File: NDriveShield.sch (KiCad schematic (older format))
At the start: 26 parts, among them Q1 NTD5867NLT4G, Q2 NTD5867NLT4G, Q3 NTD5867NLT4G, Q4 NTD5867NLT4G, Q5 NTD5867NLT4G, Q6 NTD5867NLT4G, SW1 SW_PUSHBUTTON

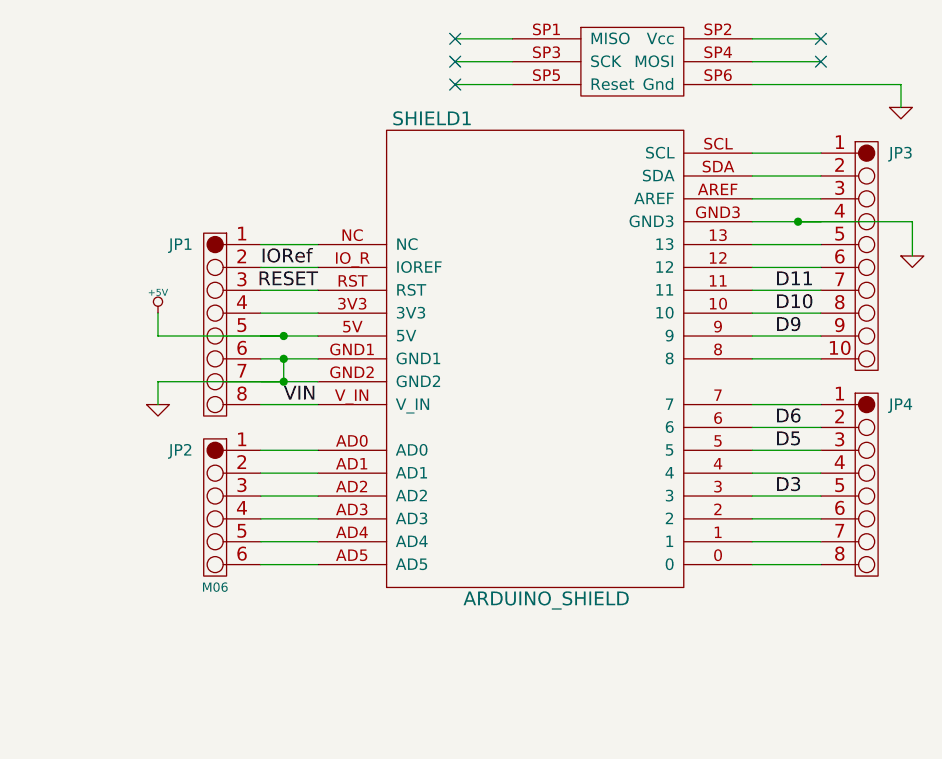
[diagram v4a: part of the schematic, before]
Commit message: Bump to V1.1, change appearance to FT-style breakout pads.
Closes #2
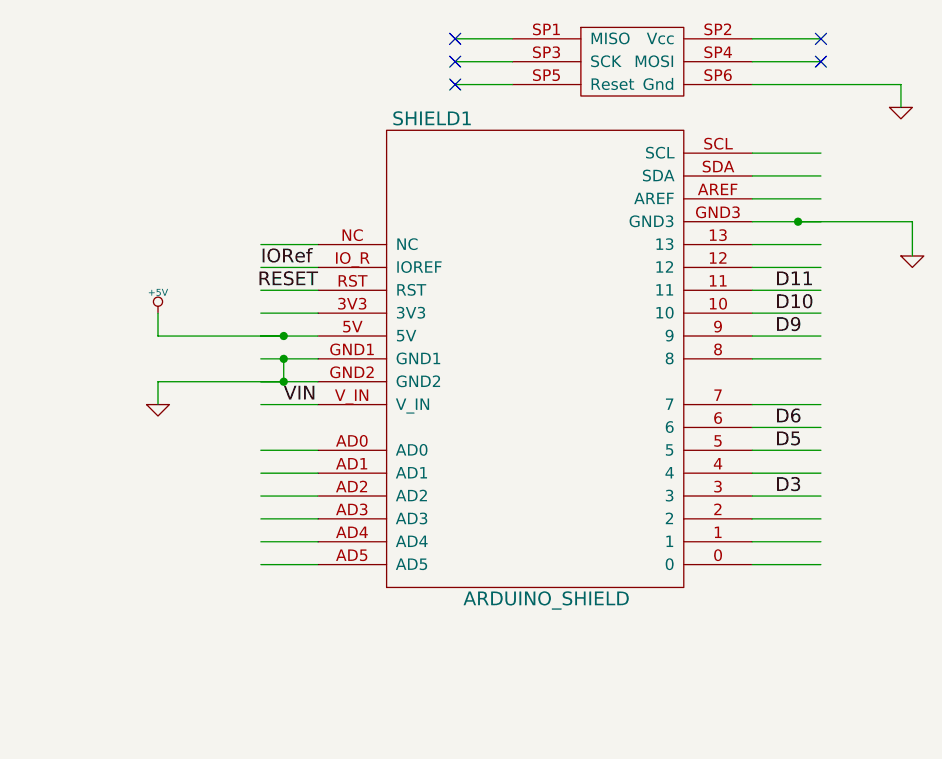
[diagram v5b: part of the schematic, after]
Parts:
- removed JP1, JP4: M08, symbol M08
- removed JP2: M06, symbol M06
- removed JP3: M10, symbol M10
- JP5: footprint (none) -> FT:TERMINALBLOCK_3.5MM_8
- LED1, LED2, LED3, LED4, LED5, LED6, LED7: footprint (none) -> FT:LED-0603
- Q1, Q2, Q3, Q4, Q5, Q6: footprint (none) -> FT:MOSFET_DPAK
- R1, R2, R3, R4, R5, R6: footprint (none) -> FT:RES_CAY16
- SHIELD1: footprint (none) -> FT:ARDUINO_SHIELD_ROUNDPADS_BREAKOUT
- SW1: footprint (none) -> FT:TACTILE_SWITCH_SMD_2PIN_TINY
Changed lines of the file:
@@
 EESchema Schematic File Version 2
-LIBS:freetronics_kicad_sch_lib
+LIBS:freetronics_schematic
 LIBS:power
 LIBS:device
@@
 F 0 "SHIELD1" H 8800 3800 60  0000 C CNN
 F 1 "ARDUINO_SHIELD" H 9300 1700 60  0000 C CNN
-F 2 "" H 9250 2650 60  0000 C CNN
+F 2 "FT:ARDUINO_SHIELD_ROUNDPADS_BREAKOUT" H 9250 2650 60  0001 C CNN
 F 3 "" H 9250 2650 60  0000 C CNN
 	1    9250 2650
 	1    0    0    -1
-$EndComp
-$Comp
-L M08 JP4
-U 1 1 53BDDB94
-P 10800 2750
-F 0 "JP4" H 10850 2750 50  0000 C CNN
-F 1 "M08" H 10700 1950 40  0001 C CNN
-F 2 "" H 10800 2750 60  0000 C CNN
-F 3 "" H 10800 2750 60  0000 C CNN
-	1    10800 2750
-	1    0    0    -1
-$EndComp
-$Comp
-L M10 JP3
-U 1 1 53BDDBD8
-P 10800 1650
-F 0 "JP3" H 10850 1650 50  0000 C CNN
-F 1 "M10" H 10700 650 40  0001 C CNN
-F 2 "" H 10800 1650 60  0000 C CNN
-F 3 "" H 10800 1650 60  0000 C CNN
-	1    10800 1650
-	1    0    0    -1
-$EndComp
-$Comp
-L M06 JP2
-U 1 1 53BDDD8A
-P 7750 2950
-F 0 "JP2" H 7800 2950 50  0000 C CNN
-F 1 "M06" H 7650 2350 40  0000 C CNN
-F 2 "" H 7750 2950 60  0000 C CNN
-F 3 "" H 7750 2950 60  0000 C CNN
-	1    7750 2950
-	-1   0    0    -1
-$EndComp
-$Comp
-L M08 JP1
-U 1 1 53BDDE77
-P 7750 2050
-F 0 "JP1" H 7800 2050 50  0000 C CNN
-F 1 "M08" H 7650 1250 40  0001 C CNN
-F 2 "" H 7750 2050 60  0000 C CNN
-F 3 "" H 7750 2050 60  0000 C CNN
-	1    7750 2050
-	-1   0    0    -1
 $EndComp
 Text Label 10300 3150 0    60   ~ 0
@@
 F 0 "JP5" H 1050 1650 50  0000 C CNN
 F 1 "M08" H 1050 750 40  0000 C CNN
-F 2 "" H 1150 1550 60  0000 C CNN
+F 2 "FT:TERMINALBLOCK_3.5MM_8" H 1150 1550 60  0001 C CNN
 F 3 "" H 1150 1550 60  0000 C CNN
 	1    1150 1550
@@
 F 0 "LED1" H 3850 2700 50  0000 C CNN
 F 1 "LED" H 3850 2500 50  0000 C CNN
-F 2 "" H 3850 2600 60  0000 C CNN
+F 2 "FT:LED-0603" H 3850 2400 60  0001 C CNN
 F 3 "" H 3850 2600 60  0000 C CNN
 	1    3850 2600
@@
 F 0 "R1" H 3350 1700 50  0000 C CNN
 F 1 "1K" H 3350 1800 50  0000 C CNN
-F 2 "" H 3350 1800 60  0000 C CNN
+F 2 "FT:RES_CAY16" H 3350 1800 60  0001 C CNN
 F 3 "" H 3350 1800 60  0000 C CNN
 	1    3350 1800
@@
 F 0 "R3" H 3850 2250 50  0000 C CNN
 F 1 "10K" H 3850 2150 50  0000 C CNN
-F 2 "" H 3850 2150 60  0000 C CNN
+F 2 "FT:RES_CAY16" H 3850 2150 60  0001 C CNN
 F 3 "" H 3850 2150 60  0000 C CNN
 	1    3850 2150
@@
 F 0 "R2" H 3050 2250 50  0000 C CNN
 F 1 "470R" H 3050 2150 50  0000 C CNN
-F 2 "" H 3050 2150 60  0000 C CNN
+F 2 "FT:RES_CAY16" H 3050 2150 60  0001 C CNN
 F 3 "" H 3050 2150 60  0000 C CNN
 	3    3050 2150
@@
 F 0 "Q1" H 4000 1700 60  0000 R CNN
 F 1 "NTD5867NLT4G" V 4400 2050 60  0000 R CNN
-F 2 "" H 4100 1800 60  0000 C CNN
+F 2 "FT:MOSFET_DPAK" H 4100 1800 60  0001 C CNN
 F 3 "" H 4100 1800 60  0000 C CNN
 	1    4100 1800
@@
 F 0 "LED2" H 3850 4350 50  0000 C CNN
 F 1 "LED" H 3850 4150 50  0000 C CNN
-F 2 "" H 3850 4250 60  0000 C CNN
+F 2 "FT:LED-0603" H 3850 4250 60  0001 C CNN
 F 3 "" H 3850 4250 60  0000 C CNN
 	1    3850 4250
@@
 F 0 "R1" H 3350 3350 50  0000 C CNN
 F 1 "1K" H 3350 3450 50  0000 C CNN
-F 2 "" H 3350 3450 60  0000 C CNN
+F 2 "FT:RES_CAY16" H 3350 3450 60  0001 C CNN
 F 3 "" H 3350 3450 60  0000 C CNN
 	2    3350 3450
@@
 F 0 "R3" H 3850 3900 50  0000 C CNN
 F 1 "10K" H 3850 3800 50  0000 C CNN
-F 2 "" H 3850 3800 60  0000 C CNN
+F 2 "FT:RES_CAY16" H 3850 3800 60  0001 C CNN
 F 3 "" H 3850 3800 60  0000 C CNN
 	2    3850 3800
@@
 F 0 "R2" H 3050 3900 50  0000 C CNN
 F 1 "470R" H 3050 3800 50  0000 C CNN
-F 2 "" H 3050 3800 60  0000 C CNN
+F 2 "FT:RES_CAY16" H 3050 3800 60  0001 C CNN
 F 3 "" H 3050 3800 60  0000 C CNN
 	2    3050 3800
@@
 F 0 "Q2" H 4000 3350 60  0000 R CNN
 F 1 "NTD5867NLT4G" V 4400 3700 60  0000 R CNN
-F 2 "" H 4100 3450 60  0000 C CNN
+F 2 "FT:MOSFET_DPAK" H 4100 3450 60  0001 C CNN
 F 3 "" H 4100 3450 60  0000 C CNN
 	1    4100 3450
@@
 F 0 "LED4" H 6050 2700 50  0000 C CNN
 F 1 "LED" H 6050 2500 50  0000 C CNN
-F 2 "" H 6050 2600 60  0000 C CNN
+F 2 "FT:LED-0603" H 6050 2400 60  0001 C CNN
 F 3 "" H 6050 2600 60  0000 C CNN
 	1    6050 2600
@@
 F 0 "R1" H 5550 1700 50  0000 C CNN
 F 1 "1K" H 5550 1800 50  0000 C CNN
-F 2 "" H 5550 1800 60  0000 C CNN
+F 2 "FT:RES_CAY16" H 5550 1800 60  0001 C CNN
 F 3 "" H 5550 1800 60  0000 C CNN
 	4    5550 1800
@@
 F 0 "R3" H 6050 2250 50  0000 C CNN
 F 1 "10K" H 6050 2150 50  0000 C CNN
-F 2 "" H 6050 2150 60  0000 C CNN
+F 2 "FT:RES_CAY16" H 6050 2150 60  0001 C CNN
 F 3 "" H 6050 2150 60  0000 C CNN
 	4    6050 2150
@@
 F 0 "R5" H 5250 2250 50  0000 C CNN
 F 1 "470R" H 5250 2150 50  0000 C CNN
-F 2 "" H 5250 2150 60  0000 C CNN
+F 2 "FT:RES_CAY16" H 5250 2150 60  0001 C CNN
 F 3 "" H 5250 2150 60  0000 C CNN
 	3    5250 2150
@@
 F 0 "Q4" H 6200 1700 60  0000 R CNN
 F 1 "NTD5867NLT4G" V 6600 2050 60  0000 R CNN
-F 2 "" H 6300 1800 60  0000 C CNN
+F 2 "FT:MOSFET_DPAK" H 6300 1800 60  0001 C CNN
 F 3 "" H 6300 1800 60  0000 C CNN
 	1    6300 1800
@@
 F 0 "LED5" H 6050 4350 50  0000 C CNN
 F 1 "LED" H 6050 4150 50  0000 C CNN
-F 2 "" H 6050 4250 60  0000 C CNN
+F 2 "FT:LED-0603" H 6050 4250 60  0001 C CNN
 F 3 "" H 6050 4250 60  0000 C CNN
 	1    6050 4250
@@
 F 0 "R4" H 5550 3350 50  0000 C CNN
 F 1 "1K" H 5550 3450 50  0000 C CNN
-F 2 "" H 5550 3450 60  0000 C CNN
+F 2 "FT:RES_CAY16" H 5550 3450 60  0001 C CNN
 F 3 "" H 5550 3450 60  0000 C CNN
 	2    5550 3450
@@
 F 0 "R6" H 6050 3900 50  0000 C CNN
 F 1 "10K" H 6050 3800 50  0000 C CNN
-F 2 "" H 6050 3800 60  0000 C CNN
+F 2 "FT:RES_CAY16" H 6050 3800 60  0001 C CNN
 F 3 "" H 6050 3800 60  0000 C CNN
 	2    6050 3800
@@
 F 0 "R5" H 5250 3900 50  0000 C CNN
 F 1 "470R" H 5250 3800 50  0000 C CNN
-F 2 "" H 5250 3800 60  0000 C CNN
+F 2 "FT:RES_CAY16" H 5250 3800 60  0001 C CNN
 F 3 "" H 5250 3800 60  0000 C CNN
 	2    5250 3800
@@
 F 0 "Q5" H 6200 3350 60  0000 R CNN
 F 1 "NTD5867NLT4G" V 6600 3700 60  0000 R CNN
-F 2 "" H 6300 3450 60  0000 C CNN
+F 2 "FT:MOSFET_DPAK" H 6300 3450 60  0001 C CNN
 F 3 "" H 6300 3450 60  0000 C CNN
 	1    6300 3450
@@
 F 0 "LED3" H 3850 6000 50  0000 C CNN
 F 1 "LED" H 3850 5800 50  0000 C CNN
-F 2 "" H 3850 5900 60  0000 C CNN
+F 2 "FT:LED-0603" H 3850 5900 60  0001 C CNN
 F 3 "" H 3850 5900 60  0000 C CNN
 	1    3850 5900
@@
 F 0 "R1" H 3350 5000 50  0000 C CNN
 F 1 "1K" H 3350 5100 50  0000 C CNN
-F 2 "" H 3350 5100 60  0000 C CNN
+F 2 "FT:RES_CAY16" H 3350 5100 60  0001 C CNN
 F 3 "" H 3350 5100 60  0000 C CNN
 	3    3350 5100
@@
 F 0 "R3" H 3850 5550 50  0000 C CNN
 F 1 "10K" H 3850 5450 50  0000 C CNN
-F 2 "" H 3850 5450 60  0000 C CNN
+F 2 "FT:RES_CAY16" H 3850 5450 60  0001 C CNN
 F 3 "" H 3850 5450 60  0000 C CNN
 	3    3850 5450
@@
 F 0 "R2" H 3050 5550 50  0000 C CNN
 F 1 "470R" H 3050 5450 50  0000 C CNN
-F 2 "" H 3050 5450 60  0000 C CNN
+F 2 "FT:RES_CAY16" H 3050 5450 60  0001 C CNN
 F 3 "" H 3050 5450 60  0000 C CNN
 	1    3050 5450
@@
 F 0 "Q3" H 4000 5000 60  0000 R CNN
 F 1 "NTD5867NLT4G" V 4400 5350 60  0000 R CNN
-F 2 "" H 4100 5100 60  0000 C CNN
+F 2 "FT:MOSFET_DPAK" H 4100 5100 60  0001 C CNN
 F 3 "" H 4100 5100 60  0000 C CNN
 	1    4100 5100
@@
 F 0 "LED6" H 6050 6000 50  0000 C CNN
 F 1 "LED" H 6050 5800 50  0000 C CNN
-F 2 "" H 6050 5900 60  0000 C CNN
+F 2 "FT:LED-0603" H 6050 5900 60  0001 C CNN
 F 3 "" H 6050 5900 60  0000 C CNN
 	1    6050 5900
@@
 F 0 "R4" H 5550 5000 50  0000 C CNN
 F 1 "1K" H 5550 5100 50  0000 C CNN
-F 2 "" H 5550 5100 60  0000 C CNN
+F 2 "FT:RES_CAY16" H 5550 5100 60  0001 C CNN
 F 3 "" H 5550 5100 60  0000 C CNN
 	1    5550 5100
@@
 F 0 "R6" H 6050 5550 50  0000 C CNN
 F 1 "10K" H 6050 5450 50  0000 C CNN
-F 2 "" H 6050 5450 60  0000 C CNN
+F 2 "FT:RES_CAY16" H 6050 5450 60  0001 C CNN
 F 3 "" H 6050 5450 60  0000 C CNN
 	1    6050 5450
@@
 F 0 "R5" H 5250 5550 50  0000 C CNN
 F 1 "470R" H 5250 5450 50  0000 C CNN
-F 2 "" H 5250 5450 60  0000 C CNN
+F 2 "FT:RES_CAY16" H 5250 5450 60  0001 C CNN
 F 3 "" H 5250 5450 60  0000 C CNN
 	1    5250 5450
@@
 F 0 "Q6" H 6200 5000 60  0000 R CNN
 F 1 "NTD5867NLT4G" V 6600 5350 60  0000 R CNN
-F 2 "" H 6300 5100 60  0000 C CNN
+F 2 "FT:MOSFET_DPAK" H 6300 5100 60  0001 C CNN
 F 3 "" H 6300 5100 60  0000 C CNN
 	1    6300 5100
@@
 F 0 "R4" H 7700 4750 50  0000 C CNN
 F 1 "1K" H 7700 4850 50  0000 C CNN
-F 2 "" H 7700 4850 60  0000 C CNN
+F 2 "FT:RES_CAY16" H 7700 4850 60  0001 C CNN
 F 3 "" H 7700 4850 60  0000 C CNN
 	3    7700 4850
@@
 F 0 "R2" H 3650 7100 50  0000 C CNN
 F 1 "470R" H 3650 7000 50  0000 C CNN
-F 2 "" H 3650 7000 60  0000 C CNN
+F 2 "FT:RES_CAY16" H 3650 7000 60  0001 C CNN
 F 3 "" H 3650 7000 60  0000 C CNN
 	4    3650 7000
@@
 F 0 "R6" H 9050 4950 50  0000 C CNN
 F 1 "10K" H 9050 4850 50  0000 C CNN
-F 2 "" H 9050 4850 60  0000 C CNN
+F 2 "FT:RES_CAY16" H 9050 4850 60  0001 C CNN
 F 3 "" H 9050 4850 60  0000 C CNN
 	3    9050 4850
@@
 F 0 "R4" H 7700 5000 50  0000 C CNN
 F 1 "1K" H 7700 5100 50  0000 C CNN
-F 2 "" H 7700 5100 60  0000 C CNN
+F 2 "FT:RES_CAY16" H 7700 5100 60  0001 C CNN
 F 3 "" H 7700 5100 60  0000 C CNN
 	4    7700 5100
@@
 F 0 "R5" H 8400 4950 50  0000 C CNN
 F 1 "470R" H 8400 4850 50  0000 C CNN
-F 2 "" H 8400 4850 60  0000 C CNN
+F 2 "FT:RES_CAY16" H 8400 4850 60  0001 C CNN
 F 3 "" H 8400 4850 60  0000 C CNN
 	4    8400 4850
@@
 F 0 "R6" H 9050 5200 50  0000 C CNN
 F 1 "10K" H 9050 5100 50  0000 C CNN
-F 2 "" H 9050 5100 60  0000 C CNN
+F 2 "FT:RES_CAY16" H 9050 5100 60  0001 C CNN
 F 3 "" H 9050 5100 60  0000 C CNN
 	4    9050 5100
@@
 F 0 "LED7" H 4250 7100 50  0000 C CNN
 F 1 "LED" H 4250 6900 50  0000 C CNN
-F 2 "" H 4250 7000 60  0000 C CNN
+F 2 "FT:LED-0603" H 4250 7000 60  0001 C CNN
 F 3 "" H 4250 7000 60  0000 C CNN
 	1    4250 7000
@@
 F 0 "SW1" H 1400 3410 50  0000 C CNN
 F 1 "SW_PUSHBUTTON" H 1550 3220 50  0000 C CNN
-F 2 "" H 1550 3300 60  0000 C CNN
+F 2 "FT:TACTILE_SWITCH_SMD_2PIN_TINY" H 1550 3300 60  0001 C CNN
 F 3 "" H 1550 3300 60  0000 C CNN
 	1    1550 3300
